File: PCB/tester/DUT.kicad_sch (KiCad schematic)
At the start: 72 parts, among them J3 6pin_hd, J4 61300621021, J5 PPTC051LFBN-RC, J6 61300511021, J7 PPTC021LFBN-RC, K1 Relay SPDT, K2 Relay SPDT, K3 Relay SPDT, Q2 PMF170XP,115, Q3 DMN63D8L-7, Q4 DMN63D8L-7, Q5 DMN63D8L-7, Q6 DMN63D8L-7, U6 THS4281, U7 THS4281, U8 THS4281, U9 ZXCT1082

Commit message: sync with main
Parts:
- R24, R25, R32: MPN ERJ-2RKF5101X -> RT0402BRD075K1L; OEPSPN OEPS020173 -> OEPS020203; Tolerance 1% -> 0.1%

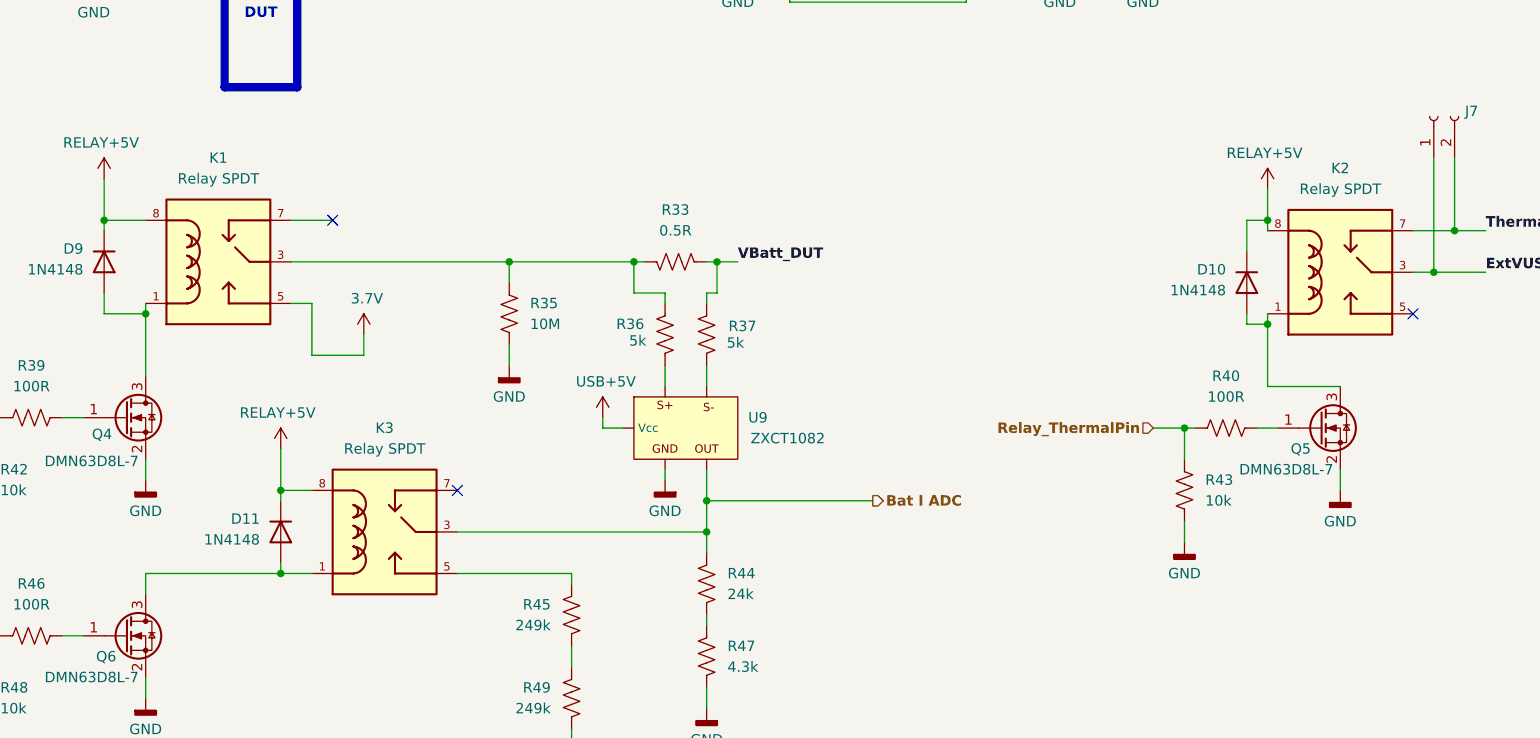
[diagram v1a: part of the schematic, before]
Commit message: início Rev.C
- corrigido pinout dos relais
- corrigido valor & MPN & OEPSPN de R13 =1R
- feito re-routing: DRC=0
- gerados ficheiros de produção
- BOM actualizada
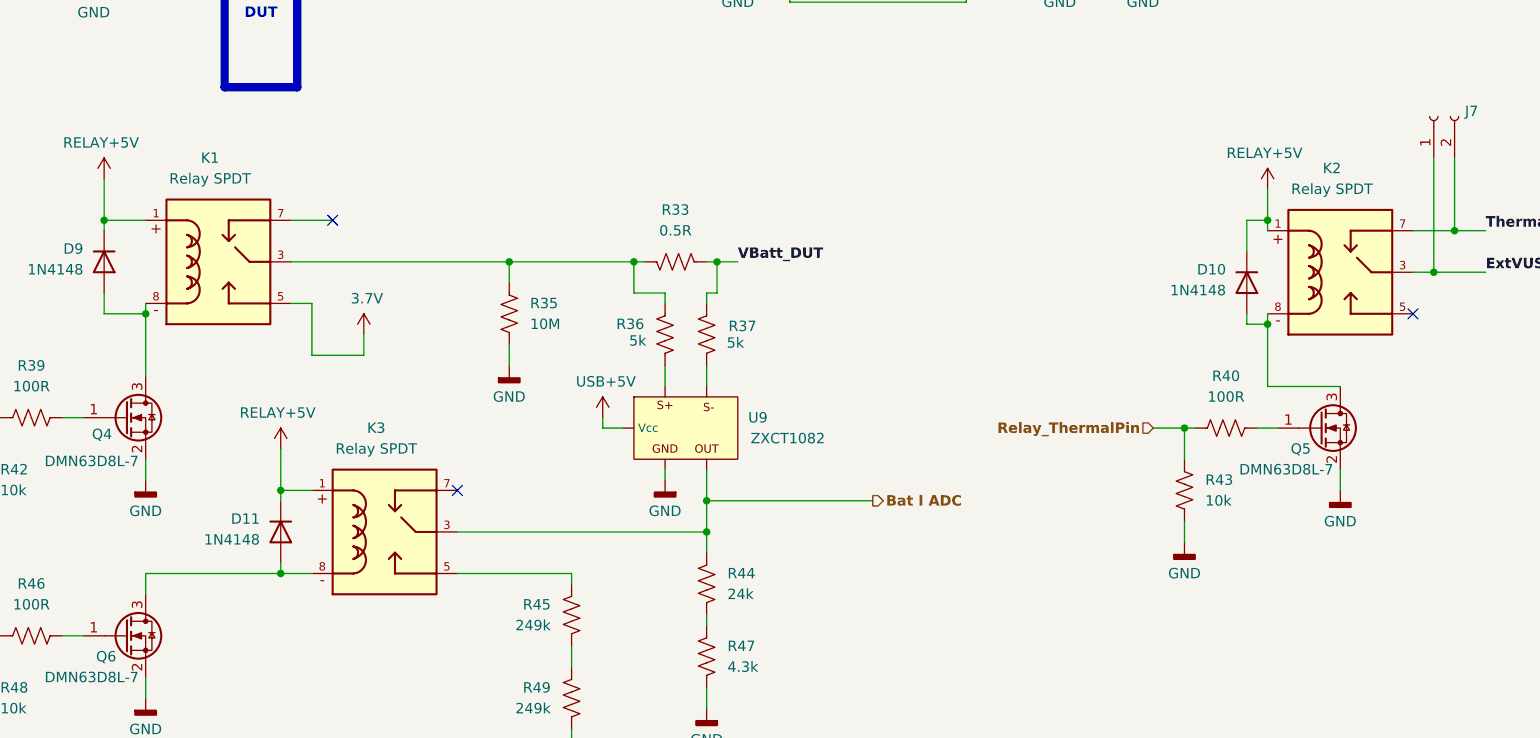
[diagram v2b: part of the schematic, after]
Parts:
- D10, D11, D9: MPN 1N4148WX-TP -> 1N4148WS-E3-18; OEPSPN OEPS030017 -> OEPS030052
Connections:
- net RELAY+5V: now also K1.1, K2.1, K3.1; no longer K1.8, K2.8, K3.8
- net at D11.2 (A), Q6.3 (D): now also K3.8; no longer K3.1
- net at D9.2 (A), Q4.3 (D): now also K1.8; no longer K1.1
- net at D10.2 (A), Q5.3 (D): now also K2.8; no longer K2.1
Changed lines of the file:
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@@
 			)
 		)
-		(property "OEPSPN" "OEPS030017"
+		(property "OEPSPN" "OEPS030052"
 			(at 71.12 162.56 90)
 			(hide yes)
@@
 			)
 		)
-		(property "MPN" "1N4148WX-TP"
+		(property "MPN" "1N4148WS-E3-18"
 			(at 71.12 162.56 90)
 			(hide yes)
@@
 			)
 		)
-		(property "OEPSPN" "OEPS030017"
+		(property "OEPSPN" "OEPS030052"
 			(at 49.53 129.54 90)
 			(hide yes)
@@
 			)
 		)
-		(property "MPN" "1N4148WX-TP"
+		(property "MPN" "1N4148WS-E3-18"
 			(at 49.53 129.54 90)
 			(hide yes)
@@
 		(fields_autoplaced yes)
 		(property "Reference" "K3"
-			(at 83.82 149.86 0)
+			(at 82.7998 149.86 0)
 			(show_name no)
 			(do_not_autoplace no)
@@
 		)
 		(property "Value" "Relay SPDT"
-			(at 83.82 152.4 0)
+			(at 82.7998 152.4 0)
 			(show_name no)
 			(do_not_autoplace no)
@@
 		)
 		(property "Footprint" "FED3_PCBLib:RELAY_1462042-8"
-			(at 82.55 162.56 0)
+			(at 81.28 164.592 0)
 			(hide yes)
 			(show_name no)
@@
 			)
 		)
-		(property "Description" "OTHER:   RELAY SPDT 2A 5V TELECOM   [1462042-8] [SMD]"
+		(property "Description" "RELAY SPDT 2A 5V TELECOM   [1462042-8] [SMD]"
 			(at 82.55 162.56 0)
 			(hide yes)
@@
 			)
 		)
-		(property "TempCo" ""
-			(at 82.55 162.56 0)
-			(hide yes)
-			(show_name no)
-			(do_not_autoplace no)
-			(effects
-				(font
-					(size 1.27 1.27)
-				)
-			)
-		)
-		(property "Tolerance" ""
-			(at 82.55 162.56 0)
-			(hide yes)
-			(show_name no)
-			(do_not_autoplace no)
-			(effects
-				(font
-					(size 1.27 1.27)
-				)
-			)
-		)
-		(property "Voltage" ""
-			(at 82.55 162.56 0)
-			(hide yes)
-			(show_name no)
-			(do_not_autoplace no)
-			(effects
-				(font
-					(size 1.27 1.27)
-				)
-			)
-		)
 		(pin "5"
 		)
@@
 			)
 		)
-		(property "OEPSPN" "OEPS030017"
+		(property "OEPSPN" "OEPS030052"
 			(at 189.23 132.08 90)
 			(hide yes)
@@
 			)
 		)
-		(property "MPN" "1N4148WX-TP"
+		(property "MPN" "1N4148WS-E3-18"
 			(at 189.23 132.08 90)
 			(hide yes)
@@
 		(fields_autoplaced yes)
 		(property "Reference" "K1"
-			(at 63.5 116.84 0)
+			(at 62.4798 116.84 0)
 			(show_name no)
 			(do_not_autoplace no)
@@
 		)
 		(property "Value" "Relay SPDT"
-			(at 63.5 119.38 0)
+			(at 62.4798 119.38 0)
 			(show_name no)
 			(do_not_autoplace no)
@@
 		)
 		(property "Footprint" "FED3_PCBLib:RELAY_1462042-8"
-			(at 62.23 129.54 0)
+			(at 60.96 131.572 0)
 			(hide yes)
 			(show_name no)
@@
 			)
 		)
-		(property "Description" "OTHER:   RELAY SPDT 2A 5V TELECOM   [1462042-8] [SMD]"
+		(property "Description" "RELAY SPDT 2A 5V TELECOM   [1462042-8] [SMD]"
 			(at 62.23 129.54 0)
 			(hide yes)
@@
 			)
 		)
-		(property "TempCo" ""
-			(at 62.23 129.54 0)
-			(hide yes)
-			(show_name no)
-			(do_not_autoplace no)
-			(effects
-				(font
-					(size 1.27 1.27)
-				)
-			)
-		)
-		(property "Tolerance" ""
-			(at 62.23 129.54 0)
-			(hide yes)
-			(show_name no)
-			(do_not_autoplace no)
-			(effects
-				(font
-					(size 1.27 1.27)
-				)
-			)
-		)
-		(property "Voltage" ""
-			(at 62.23 129.54 0)
-			(hide yes)
-			(show_name no)
-			(do_not_autoplace no)
-			(effects
-				(font
-					(size 1.27 1.27)
-				)
-			)
-		)
 		(pin "5"
 		)
@@
 		(fields_autoplaced yes)
 		(property "Reference" "K2"
-			(at 200.66 118.11 0)
+			(at 199.6398 118.11 0)
 			(show_name no)
 			(do_not_autoplace no)
@@
 		)
 		(property "Value" "Relay SPDT"
-			(at 200.66 120.65 0)
+			(at 199.6398 120.65 0)
 			(show_name no)
 			(do_not_autoplace no)
@@
 		)
 		(property "Footprint" "FED3_PCBLib:RELAY_1462042-8"
-			(at 199.39 130.81 0)
+			(at 198.12 132.842 0)
 			(hide yes)
 			(show_name no)
@@
 			)
 		)
-		(property "Description" "OTHER:   RELAY SPDT 2A 5V TELECOM   [1462042-8] [SMD]"
+		(property "Description" "RELAY SPDT 2A 5V TELECOM   [1462042-8] [SMD]"
 			(at 199.39 130.81 0)
 			(hide yes)
@@
 			(at 199.39 130.81 0)
 			(hide yes)
-			(show_name no)
-			(do_not_autoplace no)
-			(effects
-				(font
-					(size 1.27 1.27)
-				)
-			)
-		)
-		(property "TempCo" ""
-			(at 199.39 130.81 0)
-			(hide yes)
-			(show_name no)
-			(do_not_autoplace no)
-			(effects
-				(font
-					(size 1.27 1.27)
-				)
-			)
-		)
-		(property "Tolerance" ""
-			(at 199.39 130.81 0)
-			(hide yes)
-			(show_name no)
-			(do_not_autoplace no)
-			(effects
-				(font
-					(size 1.27 1.27)
-				)
-			)
-		)
-		(property "Voltage" ""
-			(at 199.39 130.81 0)
-			(hide yes)
